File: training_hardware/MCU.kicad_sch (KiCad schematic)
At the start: 2 parts, among them J1 RJ45_LED_Shielded, U1 Teensy4.1_DEV-16771

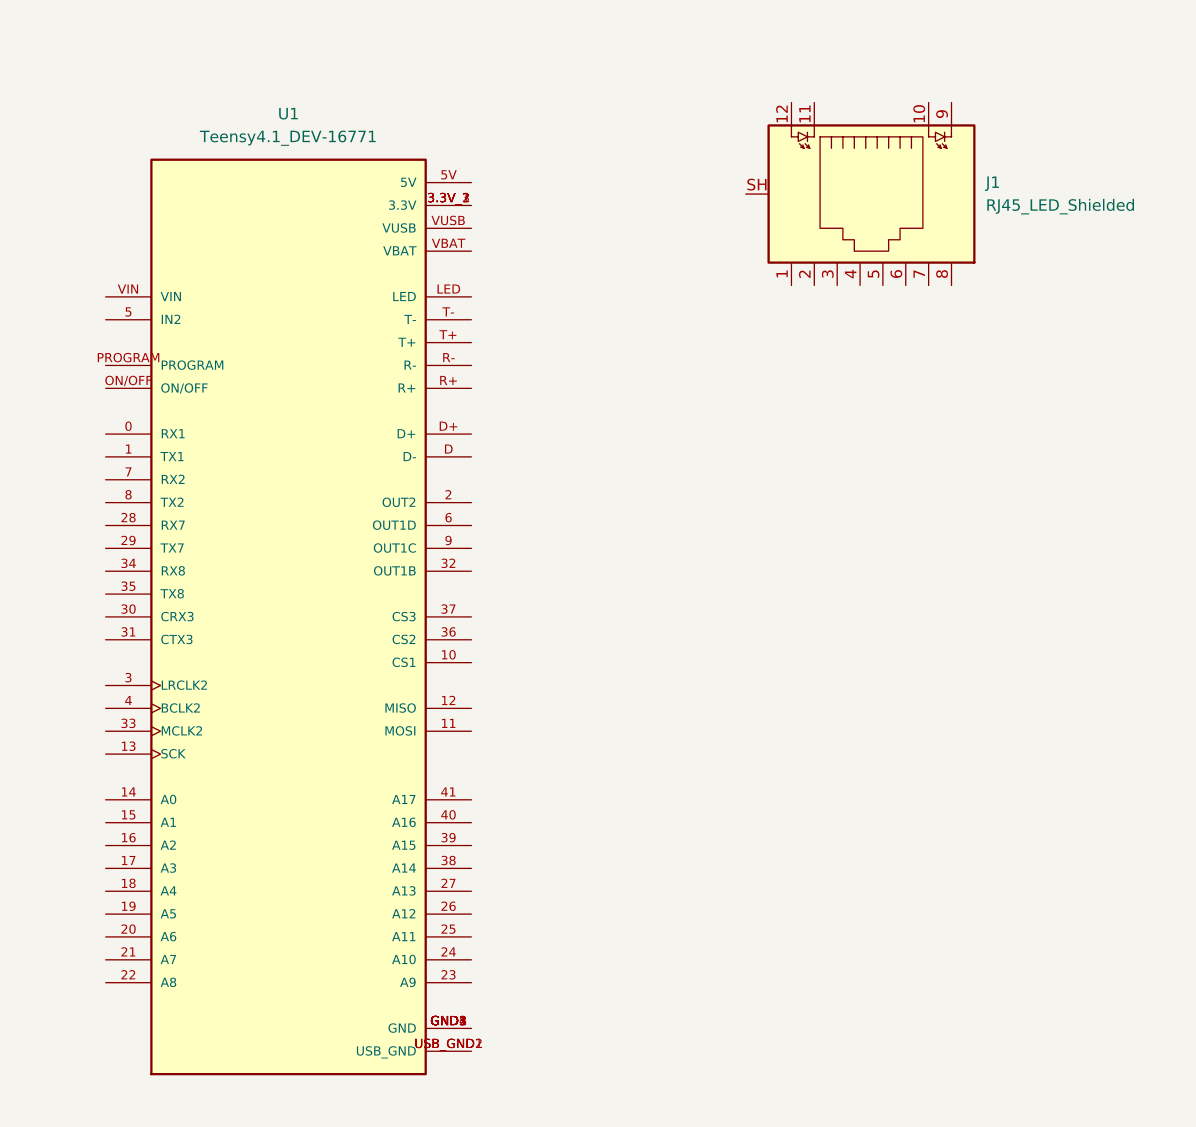
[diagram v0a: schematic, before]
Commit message: Add Ethernet
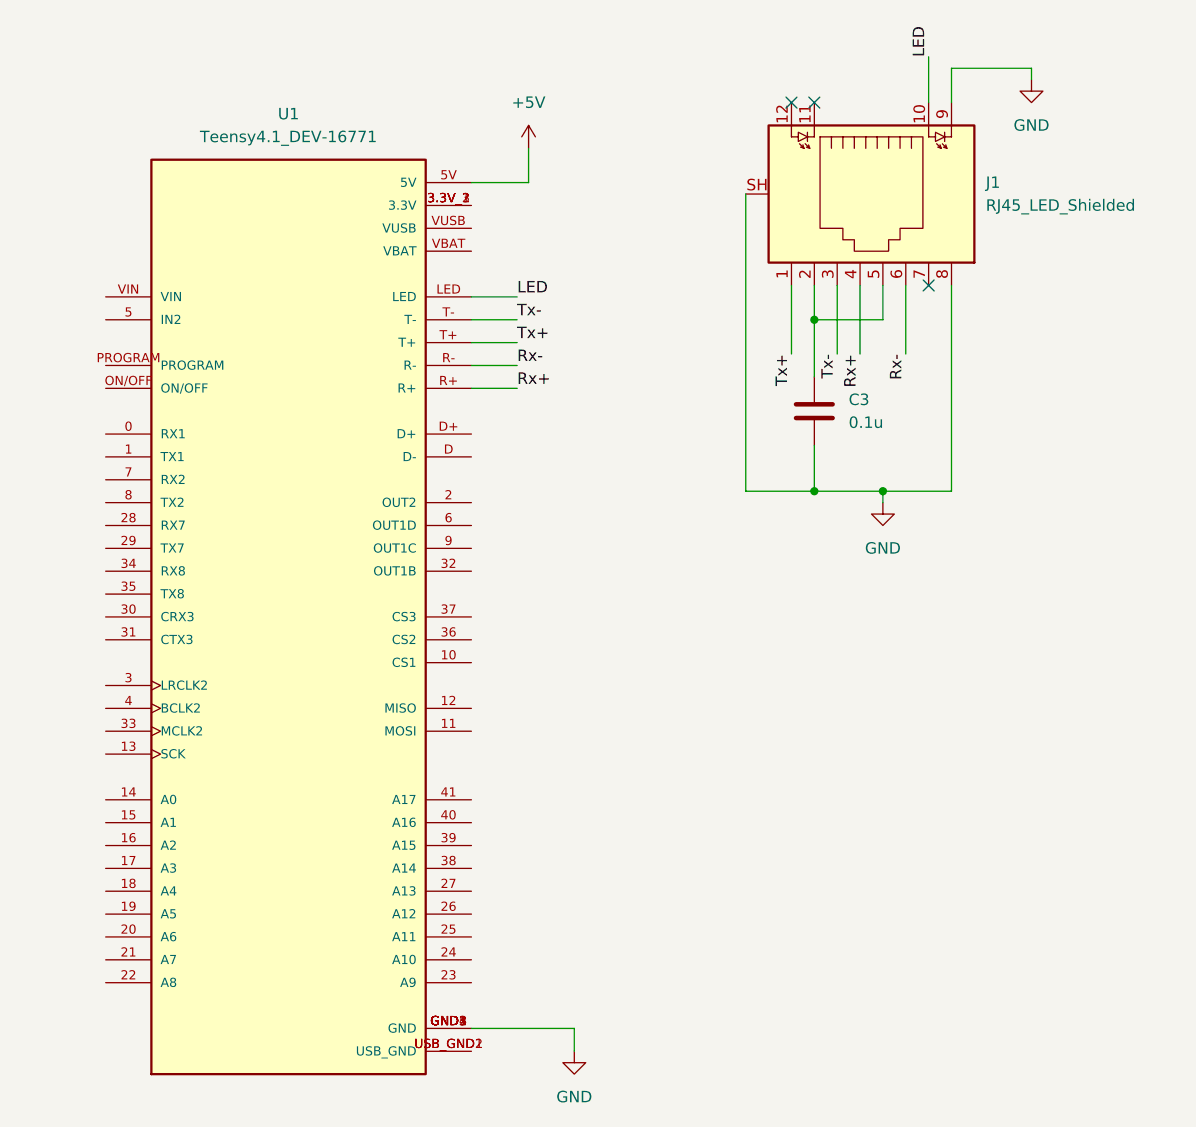
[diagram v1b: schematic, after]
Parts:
- added C3: 0.1u, symbol Device:C
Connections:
- net +5V: now reaches U1.5V
- net GND: now reaches U1.GND1 (GND), U1.GND2 (GND), U1.GND3 (GND), U1.GND4 (GND), U1.GND5 (GND)
- net GND: now also J1.8, J1.9, J1.SH, C3.2
- net LED: now reaches U1.LED
- net LED: now also J1.10
- net Rx+: now reaches U1.R+
- net Rx+: now also J1.4
- net Rx-: now reaches U1.R-
- net Rx-: now also J1.6
- net Tx+: now reaches U1.T+
- net Tx+: now also J1.1
- net Tx-: now reaches U1.T-
- net Tx-: now also J1.3
- net at J1.2: now also J1.5, C3.1
- no-connect marks 0 -> 3

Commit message: Finish Schematic
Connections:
- net STBY: now reaches U1.2 (OUT2)
- net CTX1: now reaches U1.22 (A8)
- net CRX1: now reaches U1.23 (A9)
- net +3V3: now reaches U1.3.3V_1 (3.3V), U1.3.3V_2 (3.3V), U1.3.3V_3 (3.3V)
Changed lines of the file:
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@@
+	(wire
+		(pts
+			(xy 74.93 26.67) (xy 74.93 33.02)
+		)
+		(stroke
+			(width 0)
+			(type default)
+		)
+	)
 	(wire
 		(pts
@@
 	(wire
 		(pts
+			(xy 62.23 33.02) (xy 74.93 33.02)
+		)
+		(stroke
+			(width 0)
+			(type default)
+		)
+	)
+	(wire
+		(pts
 			(xy 100.33 45.72) (xy 100.33 52.07)
 		)
@@
 	(wire
 		(pts
+			(xy 62.23 119.38) (xy 73.66 119.38)
+		)
+		(stroke
+			(width 0)
+			(type default)
+		)
+	)
+	(wire
+		(pts
 			(xy 62.23 50.8) (xy 67.31 50.8)
 		)
@@
 	(wire
 		(pts
+			(xy 62.23 66.04) (xy 67.31 66.04)
+		)
+		(stroke
+			(width 0)
+			(type default)
+		)
+	)
+	(wire
+		(pts
 			(xy 102.87 41.91) (xy 102.87 49.53)
 		)
@@
 		(pts
 			(xy 110.49 41.91) (xy 110.49 49.53)
+		)
+		(stroke
+			(width 0)
+			(type default)
+		)
+	)
+	(wire
+		(pts
+			(xy 19.05 119.38) (xy 21.59 119.38)
 		)
 		(stroke
@@
 			)
 			(justify right bottom)
+		)
+	)
+	(hierarchical_label "CRX1"
+		(shape input)
+		(at 73.66 119.38 0)
+		(effects
+			(font
+				(size 1.27 1.27)
+			)
+			(justify left)
+		)
+	)
+	(hierarchical_label "CTX1"
+		(shape output)
+		(at 19.05 119.38 180)
+		(effects
+			(font
+				(size 1.27 1.27)
+			)
+			(justify right)
+		)
+	)
+	(hierarchical_label "STBY"
+		(shape output)
+		(at 67.31 66.04 0)
+		(effects
+			(font
+				(size 1.27 1.27)
+			)
+			(justify left)
 		)
 	)
@@
 					(unit 1)
 				)
+			)
+		)
+	)
+	(symbol
+		(lib_id "power:+3V3")
+		(at 74.93 26.67 0)
+		(unit 1)
+		(exclude_from_sim no)
+		(in_bom yes)
+		(on_board yes)
+		(dnp no)
+		(fields_autoplaced yes)
+		(property "Reference" "#PWR016"
+			(at 74.93 30.48 0)
+			(effects
+				(font
+					(size 1.27 1.27)
+				)
+				(hide yes)
+			)
+		)
+		(property "Value" "+3V3"
+			(at 74.93 21.59 0)
+			(effects
+				(font
+					(size 1.27 1.27)
+				)
+			)
+		)
+		(property "Footprint" ""
+			(at 74.93 26.67 0)
+			(effects
+				(font
+					(size 1.27 1.27)
+				)
+				(hide yes)
+			)
+		)
+		(property "Datasheet" ""
+			(at 74.93 26.67 0)
+			(effects
+				(font
+					(size 1.27 1.27)
+				)
+				(hide yes)
+			)
+		)
+		(property "Description" "Power symbol creates a global label with name \"+3V3\""
+			(at 74.93 26.67 0)
+			(effects
+				(font
+					(size 1.27 1.27)
+				)
+				(hide yes)
+			)
+		)
+		(pin "1"
+		)
+		(instances
+			(project ""
+				(path "/13ce2e34-cc5b-4cfe-ac61-3c662d8291c3/de2d2a9f-7866-4fcd-b6d8-3fae1bbfdb72"
+					(reference "#PWR016")
+					(unit 1)
+				)
